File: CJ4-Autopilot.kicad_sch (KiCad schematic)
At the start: 41 parts, among them J1 CRS encoder, J2 FLC encoder, J3 HDG encoder, J4 ALT encoder, J5 CRS encoder, SW1 FD1, SW10 ALT, SW11 YD, SW12 XFR, SW13 AP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

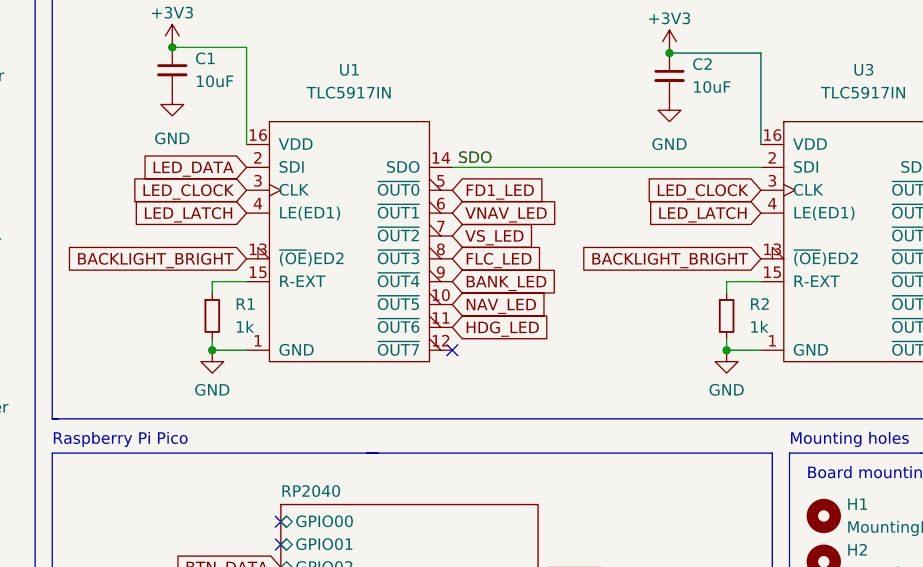
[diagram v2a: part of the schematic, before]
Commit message: Add missing net labels
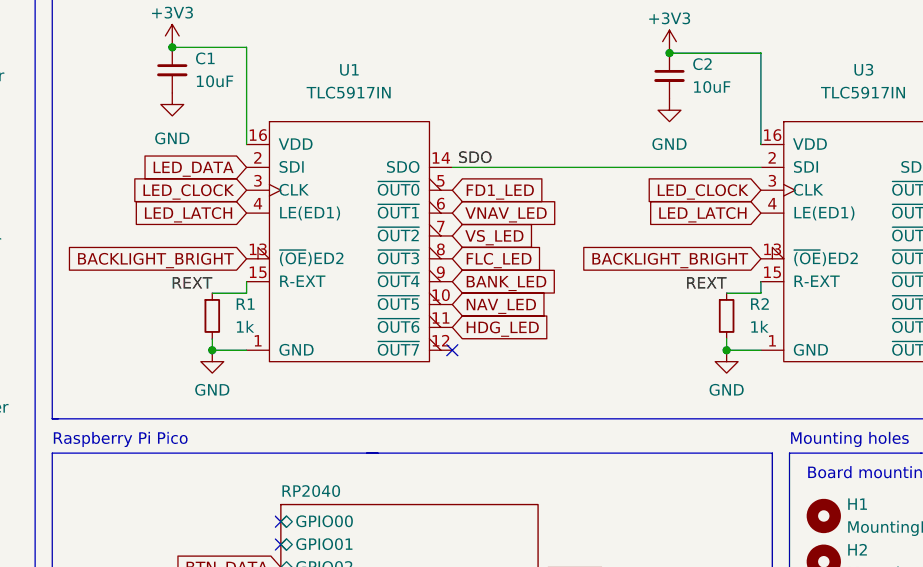
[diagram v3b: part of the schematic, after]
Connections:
- net REXT: now reaches R1.1, U1.15 (R-EXT)
- net REXT: now also R2.1, U3.15 (R-EXT)
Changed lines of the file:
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@@
+    (stroke (width 0) (type default) (color 0 0 0 0))
+  )
+  (wire (pts (xy 190.5 49.53) (xy 190.5 48.26))
     (stroke (width 0) (type default) (color 0 0 0 0))
   )
@@
     (stroke (width 0) (type default) (color 0 0 0 0))
   )
-  (wire (pts (xy 133.35 48.26) (xy 129.54 48.26))
+  (wire (pts (xy 133.35 49.53) (xy 129.54 49.53))
     (stroke (width 0) (type default) (color 0 0 0 0))
   )
@@
     (stroke (width 0) (type default) (color 0 0 0 0))
   )
-  (wire (pts (xy 186.69 48.26) (xy 186.69 49.53))
-    (stroke (width 0) (type default) (color 0 0 0 0))
-  )
   (wire (pts (xy 85.725 29.21) (xy 87.63 29.21))
     (stroke (width 0) (type default) (color 0 0 0 0))
@@
     (stroke (width 0) (type default) (color 0 0 0 0))
   )
+  (wire (pts (xy 133.35 49.53) (xy 133.35 48.26))
+    (stroke (width 0) (type default) (color 0 0 0 0))
+  )
   (polyline (pts (xy 254 108.585) (xy 254 97.79))
     (stroke (width 0) (type default) (color 0 0 0 0))
@@
     (stroke (width 0) (type default) (color 0 0 0 0))
   )
-  (wire (pts (xy 190.5 48.26) (xy 186.69 48.26))
+  (wire (pts (xy 190.5 49.53) (xy 186.69 49.53))
     (stroke (width 0) (type default) (color 0 0 0 0))
   )
@@
     (stroke (width 0) (type default) (color 0 0 0 0))
   )
-  (wire (pts (xy 129.54 48.26) (xy 129.54 49.53))
-    (stroke (width 0) (type default) (color 0 0 0 0))
-  )
   (wire (pts (xy 81.28 115.57) (xy 79.375 115.57))
     (stroke (width 0) (type default) (color 0 0 0 0))
@@
     (effects (font (size 1.27 1.27)) (justify left bottom))
   )
+  (label "REXT" (at 186.69 49.53 180)
+    (effects (font (size 1.27 1.27)) (justify right bottom))
+  )
+  (label "REXT" (at 129.54 49.53 180)
+    (effects (font (size 1.27 1.27)) (justify right bottom))
+  )
   (label "SDO" (at 156.845 35.56 0)
